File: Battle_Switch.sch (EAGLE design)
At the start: 10 parts, among them IC1 ATTINY13A

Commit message: Added mode and threshold select jumpers.
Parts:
- added SJ1, SJ2: JUMPER-PTH-3-2OF3_NC, Battle_Switch:JUMPER-PTH-3-2OF3_NC
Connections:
- new net THRESH_SEL: SJ2.1
- net GND: now also SJ1.2, SJ2.2
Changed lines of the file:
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@@
 <part name="R1" library="Battle_Switch" deviceset="RESISTOR" device="" value="10k"/>
 <part name="R2" library="Battle_Switch" deviceset="RESISTOR" device="" value="10k"/>
+<part name="SJ2" library="Battle_Switch" deviceset="JUMPER-PTH-3-2OF3_NC" device=""/>
+<part name="GND5" library="Battle_Switch" deviceset="GND" device=""/>
+<part name="SJ1" library="Battle_Switch" deviceset="JUMPER-PTH-3-2OF3_NC" device=""/>
+<part name="GND6" library="Battle_Switch" deviceset="GND" device=""/>
 </parts>
 <sheets>
@@
 <instance part="R1" gate="G$1" x="-12.7" y="-30.48" rot="MR270"/>
 <instance part="R2" gate="G$1" x="12.7" y="-30.48" rot="R270"/>
+<instance part="SJ2" gate="G$1" x="-144.78" y="-40.64" rot="R270"/>
+<instance part="GND5" gate="G$1" x="-149.86" y="-30.48"/>
+<instance part="SJ1" gate="G$1" x="-144.78" y="-25.4" rot="R270"/>
+<instance part="GND6" gate="G$1" x="-149.86" y="-45.72"/>
 </instances>
 <busses>
@@
 <junction x="5.08" y="-40.64"/>
 </segment>
+<segment>
+<pinref part="GND5" gate="G$1" pin="GND"/>
+<wire x1="-149.86" y1="-27.94" x2="-149.86" y2="-25.4" width="0.1524" layer="91"/>
+<pinref part="SJ1" gate="G$1" pin="2"/>
+<wire x1="-149.86" y1="-25.4" x2="-147.32" y2="-25.4" width="0.1524" layer="91"/>
+</segment>
+<segment>
+<pinref part="SJ2" gate="G$1" pin="2"/>
+<wire x1="-147.32" y1="-40.64" x2="-149.86" y2="-40.64" width="0.1524" layer="91"/>
+<wire x1="-149.86" y1="-40.64" x2="-149.86" y2="-43.18" width="0.1524" layer="91"/>
+<pinref part="GND6" gate="G$1" pin="GND"/>
+</segment>
 </net>
 <net name="VIN" class="0">
@@
 </segment>
 </net>
+<net name="MODE_SEL" class="0">
+<segment>
+<wire x1="-147.32" y1="-22.86" x2="-149.86" y2="-22.86" width="0.1524" layer="91"/>
+<label x="-149.86" y="-22.86" size="1.016" layer="95" rot="R180" xref="yes"/>
+</segment>
+</net>
+<net name="THRESH_SEL" class="0">
+<segment>
+<pinref part="SJ2" gate="G$1" pin="1"/>
+<wire x1="-147.32" y1="-38.1" x2="-149.86" y2="-38.1" width="0.1524" layer="91"/>
+<label x="-149.86" y="-38.1" size="1.016" layer="95" rot="R180" xref="yes"/>
+</segment>
+</net>

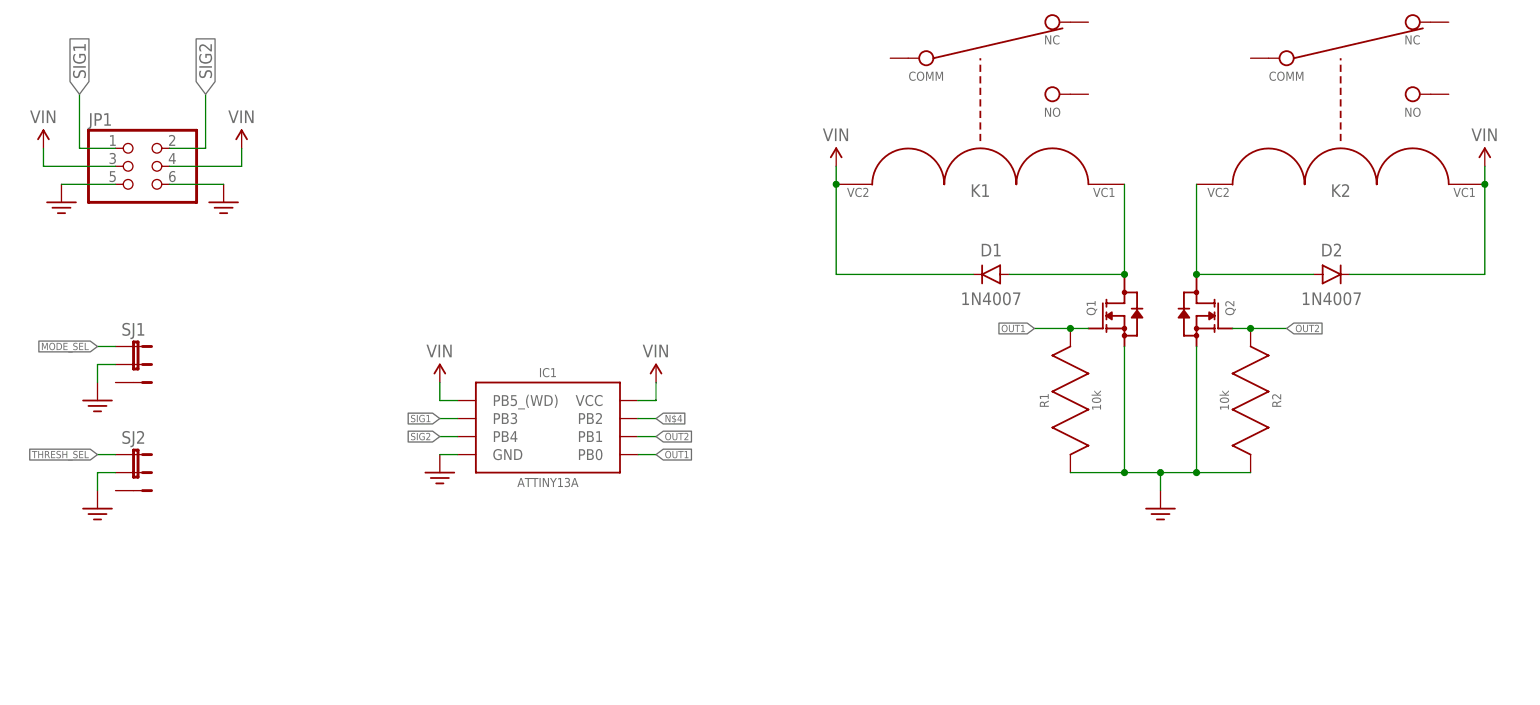
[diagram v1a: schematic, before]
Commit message: Completed board layout.  Ready for copper ground pour.
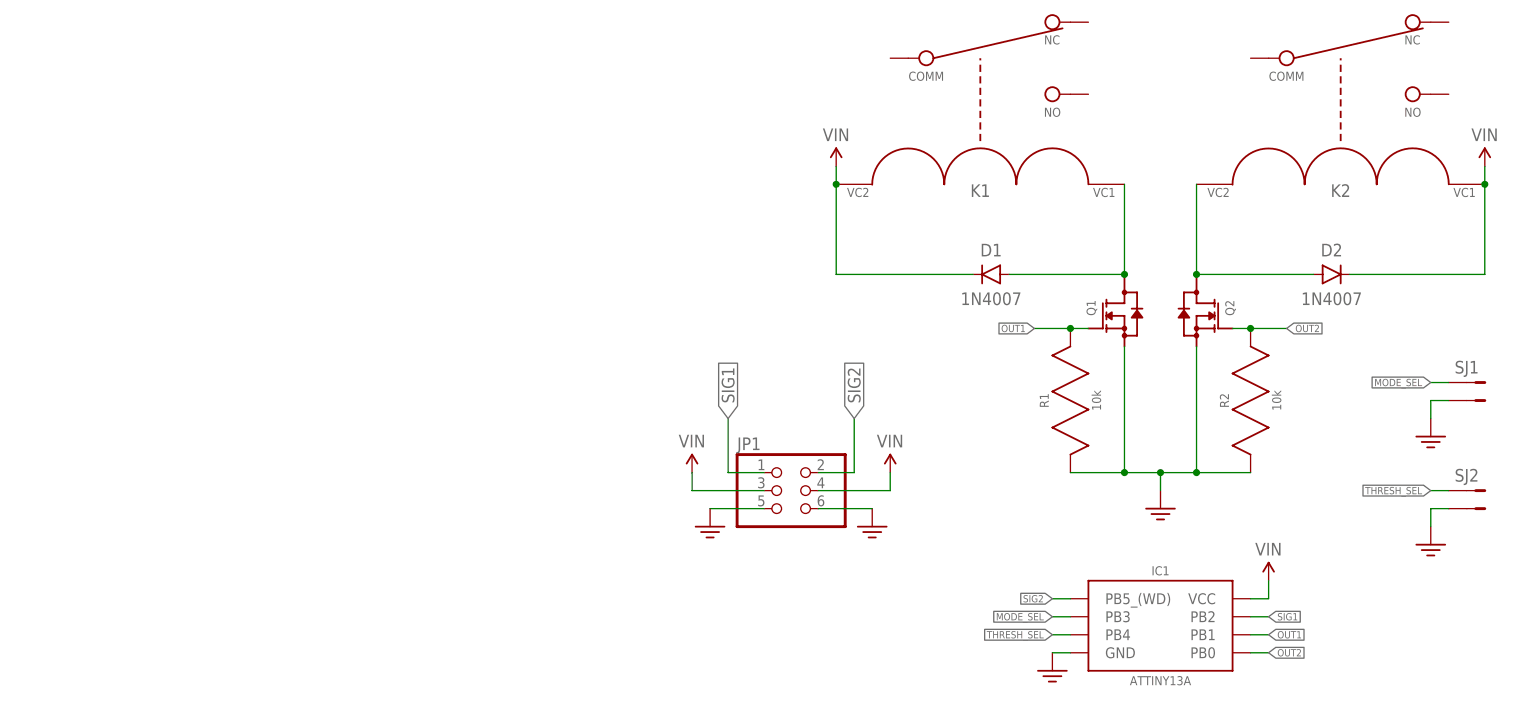
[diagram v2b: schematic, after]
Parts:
- SJ1, SJ2: value JUMPER-PTH-3-2OF3_NC -> (none); device Battle_Switch:JUMPER-PTH-3-2OF3_NC -> Battle_Switch:JUMPER-PTH-2-NO
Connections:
- removed net GND: IC1.GND, JP1.5, JP1.6, Q1.SOURCE, Q2.SOURCE, R1.P$2, R2.P$2, SJ1.2, SJ2.2
- removed net VIN: D1.C, D2.C, IC1.PB5_(WD), IC1.VCC, JP1.3, JP1.4, K1.VC2, K2.VC1
- new net MODE_SEL: IC1.PB3, SJ1.1
- new net N$5: D1.C, D2.C, IC1.VCC, JP1.3, JP1.4, K1.VC2, K2.VC1
- net N$4: now also IC1.GND, JP1.5, JP1.6, Q1.SOURCE, Q2.SOURCE, R1.P$2, R2.P$1, SJ1.2, SJ2.2; no longer IC1.PB2
- net OUT1: now also IC1.PB1; no longer IC1.PB0
- net OUT2: now also IC1.PB0, R2.P$2; no longer IC1.PB1, R2.P$1
- net SIG1: now also IC1.PB2; no longer IC1.PB3
- net SIG2: now also IC1.PB5_(WD); no longer IC1.PB4
- net THRESH_SEL: now also IC1.PB4
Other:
- moved on the sheet: IC1, JP1, R2

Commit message: Revision A layout complete.  Ready for silkscreen additions.
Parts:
- renumbered JP1 to INPUT, SJ1 to MODE_SEL, SJ2 to THRESH_SEL
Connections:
- net N$4 renamed GND
- net N$5 renamed VIN
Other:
- moved on the sheet: R1, R2
